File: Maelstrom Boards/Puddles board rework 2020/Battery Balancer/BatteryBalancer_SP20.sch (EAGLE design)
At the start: 84 parts, among them IC3 REG1117, P2 39-30-16, Q1 SPB80P06P, Q10 MOSFET-NCH-AO3404A, Q11 MOSFET-NCH-AO3404A, Q19 FDD4141TO252, Q2 SPB80P06P, Q22 FDD4141TO252, Q3 NMOSFET-D2PAK-7, Q4 310mA/60V/1.6Ω, Q5 NMOSFET-D2PAK-7, Q6 FDD4141TO252, Q7 MOSFET-NCH-AO3404A, Q8 MOSFET-NCH-AO3404A, Q9 MOSFET-NCH-AO3404A

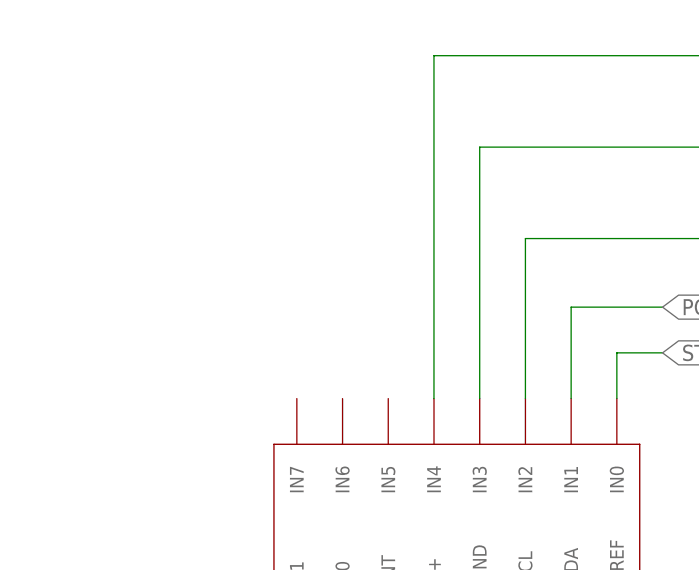
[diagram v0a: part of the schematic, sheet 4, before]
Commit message: final commit for ESC board, resistor values changed across boards for order ease
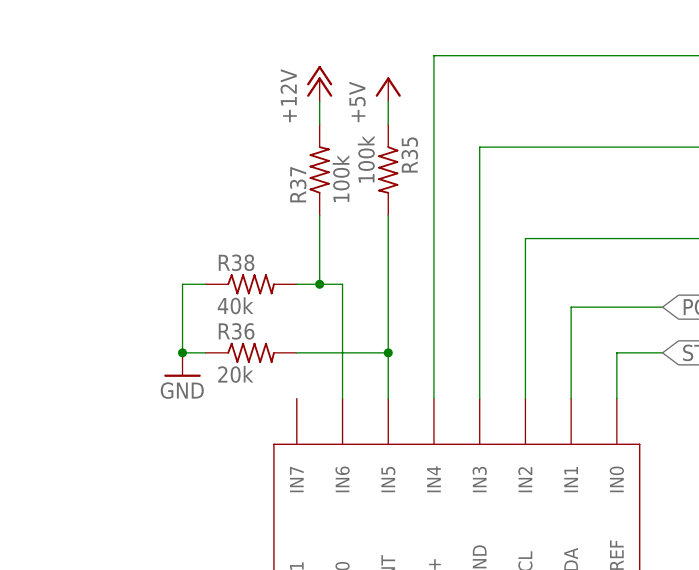
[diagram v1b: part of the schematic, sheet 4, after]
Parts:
- added R35, R37: 100k, rcl:R-US_R0603
- added R36: 20k, rcl:R-US_R0603
- added R38: 40k, rcl:R-US_R0603
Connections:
- new net N$31: R37.1, R38.2, U$12.IN6
- new net N$32: R35.2, R36.2, U$12.IN5
- net +12V: now also R37.2
- net +5V: now also R35.1
- net GND: now also R36.1, R38.1
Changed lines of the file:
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@@
 <part name="U$13" library="Vertical_Connectors" deviceset="6PIN-VERT" device=""/>
 <part name="GND26" library="supply1" library_urn="urn:adsk.eagle:library:371" deviceset="GND" device=""/>
+<part name="R35" library="rcl" library_urn="urn:adsk.eagle:library:334" deviceset="R-US_" device="R0603" package3d_urn="urn:adsk.eagle:package:23555/2" value="100k"/>
+<part name="R36" library="rcl" library_urn="urn:adsk.eagle:library:334" deviceset="R-US_" device="R0603" package3d_urn="urn:adsk.eagle:package:23555/2" value="20k"/>
+<part name="R37" library="rcl" library_urn="urn:adsk.eagle:library:334" deviceset="R-US_" device="R0603" package3d_urn="urn:adsk.eagle:package:23555/2" value="100k"/>
+<part name="R38" library="rcl" library_urn="urn:adsk.eagle:library:334" deviceset="R-US_" device="R0603" package3d_urn="urn:adsk.eagle:package:23555/2" value="40k"/>
+<part name="P+3" library="supply1" library_urn="urn:adsk.eagle:library:371" deviceset="+12V" device=""/>
+<part name="P+13" library="supply1" library_urn="urn:adsk.eagle:library:371" deviceset="+5V" device=""/>
+<part name="GND27" library="supply1" library_urn="urn:adsk.eagle:library:371" deviceset="GND" device=""/>
 </parts>
 <sheets>
@@
 <attribute name="VALUE" x="287.02" y="154.94" size="1.778" layer="96"/>
 </instance>
+<instance part="R35" gate="G$1" x="190.5" y="160.02" smashed="yes" rot="R270">
+<attribute name="NAME" x="191.9986" y="163.83" size="1.778" layer="95" rot="R270"/>
+<attribute name="VALUE" x="187.198" y="163.83" size="1.778" layer="96" rot="R270"/>
+</instance>
+<instance part="R36" gate="G$1" x="175.26" y="139.7" smashed="yes">
+<attribute name="NAME" x="171.45" y="141.1986" size="1.778" layer="95"/>
+<attribute name="VALUE" x="171.45" y="136.398" size="1.778" layer="96"/>
+</instance>
+<instance part="R37" gate="G$1" x="182.88" y="160.02" smashed="yes" rot="R90">
+<attribute name="NAME" x="181.3814" y="156.21" size="1.778" layer="95" rot="R90"/>
+<attribute name="VALUE" x="186.182" y="156.21" size="1.778" layer="96" rot="R90"/>
+</instance>
+<instance part="R38" gate="G$1" x="175.26" y="147.32" smashed="yes">
+<attribute name="NAME" x="171.45" y="148.8186" size="1.778" layer="95"/>
+<attribute name="VALUE" x="171.45" y="144.018" size="1.778" layer="96"/>
+</instance>
+<instance part="P+3" gate="1" x="182.88" y="170.18" smashed="yes">
+<attribute name="VALUE" x="180.34" y="165.1" size="1.778" layer="96" rot="R90"/>
+</instance>
+<instance part="P+13" gate="1" x="190.5" y="170.18" smashed="yes">
+<attribute name="VALUE" x="187.96" y="165.1" size="1.778" layer="96" rot="R90"/>
+</instance>
+<instance part="GND27" gate="1" x="167.64" y="137.16" smashed="yes">
+<attribute name="VALUE" x="165.1" y="134.62" size="1.778" layer="96"/>
+</instance>
 </instances>
 <busses>
@@
 <pinref part="GND5" gate="1" pin="GND"/>
 </segment>
+<segment>
+<pinref part="R36" gate="G$1" pin="1"/>
+<wire x1="170.18" y1="139.7" x2="167.64" y2="139.7" width="0.1524" layer="91"/>
+<pinref part="R38" gate="G$1" pin="1"/>
+<wire x1="167.64" y1="139.7" x2="167.64" y2="147.32" width="0.1524" layer="91"/>
+<wire x1="167.64" y1="147.32" x2="170.18" y2="147.32" width="0.1524" layer="91"/>
+<pinref part="GND27" gate="1" pin="GND"/>
+<junction x="167.64" y="139.7"/>
+</segment>
 </net>
 <net name="PORT_BATTERY" class="0">
@@
 </segment>
 </net>
+<net name="N$31" class="0">
+<segment>
+<pinref part="R38" gate="G$1" pin="2"/>
+<wire x1="180.34" y1="147.32" x2="182.88" y2="147.32" width="0.1524" layer="91"/>
+<pinref part="R37" gate="G$1" pin="1"/>
+<wire x1="182.88" y1="147.32" x2="182.88" y2="154.94" width="0.1524" layer="91"/>
+<pinref part="U$12" gate="G$1" pin="IN6"/>
+<wire x1="185.42" y1="134.62" x2="185.42" y2="147.32" width="0.1524" layer="91"/>
+<wire x1="185.42" y1="147.32" x2="182.88" y2="147.32" width="0.1524" layer="91"/>
+<junction x="182.88" y="147.32"/>
+</segment>
+</net>
+<net name="N$32" class="0">
+<segment>
+<pinref part="R35" gate="G$1" pin="2"/>
+<wire x1="190.5" y1="154.94" x2="190.5" y2="139.7" width="0.1524" layer="91"/>
+<pinref part="R36" gate="G$1" pin="2"/>
+<wire x1="190.5" y1="139.7" x2="180.34" y2="139.7" width="0.1524" layer="91"/>
+<pinref part="U$12" gate="G$1" pin="IN5"/>
+<wire x1="190.5" y1="134.62" x2="190.5" y2="139.7" width="0.1524" layer="91"/>
+<junction x="190.5" y="139.7"/>
+</segment>
+</net>
+<net name="+12V" class="0">
+<segment>
+<pinref part="R37" gate="G$1" pin="2"/>
+<pinref part="P+3" gate="1" pin="+12V"/>
+<wire x1="182.88" y1="167.64" x2="182.88" y2="165.1" width="0.1524" layer="91"/>
+</segment>
+</net>
+<net name="+5V" class="0">
+<segment>
+<pinref part="R35" gate="G$1" pin="1"/>
+<pinref part="P+13" gate="1" pin="+5V"/>
+<wire x1="190.5" y1="167.64" x2="190.5" y2="165.1" width="0.1524" layer="91"/>
+</segment>
+</net>

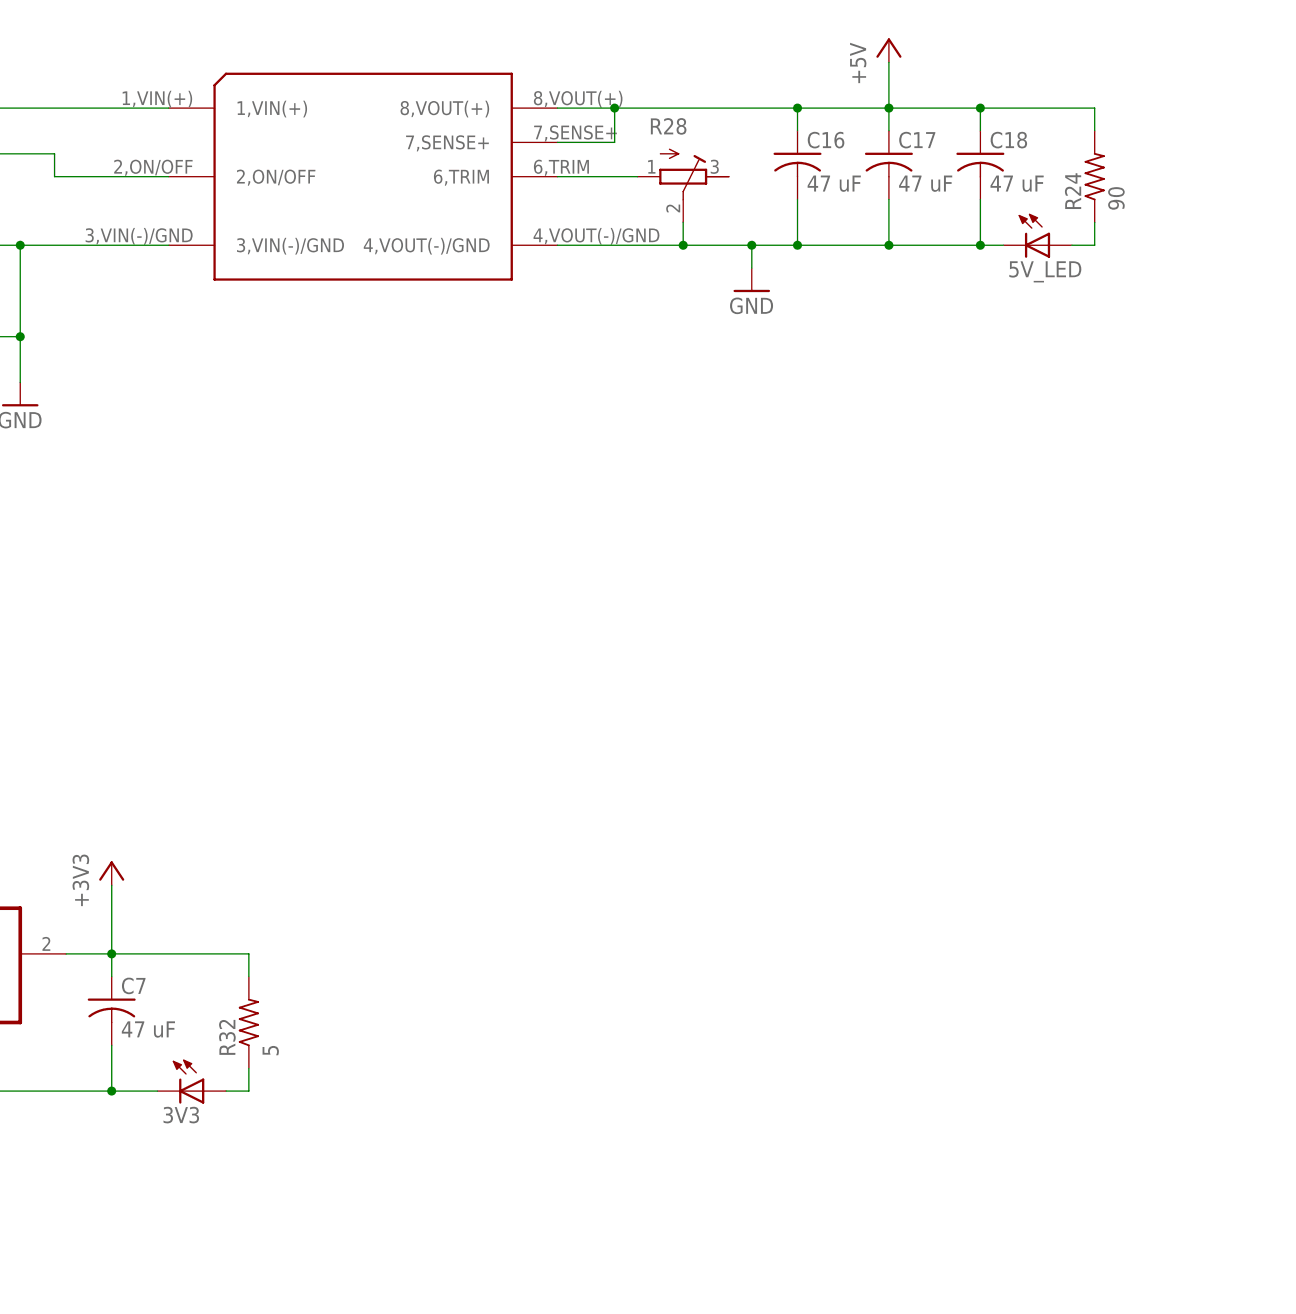
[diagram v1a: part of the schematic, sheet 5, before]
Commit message: Changing puddles values
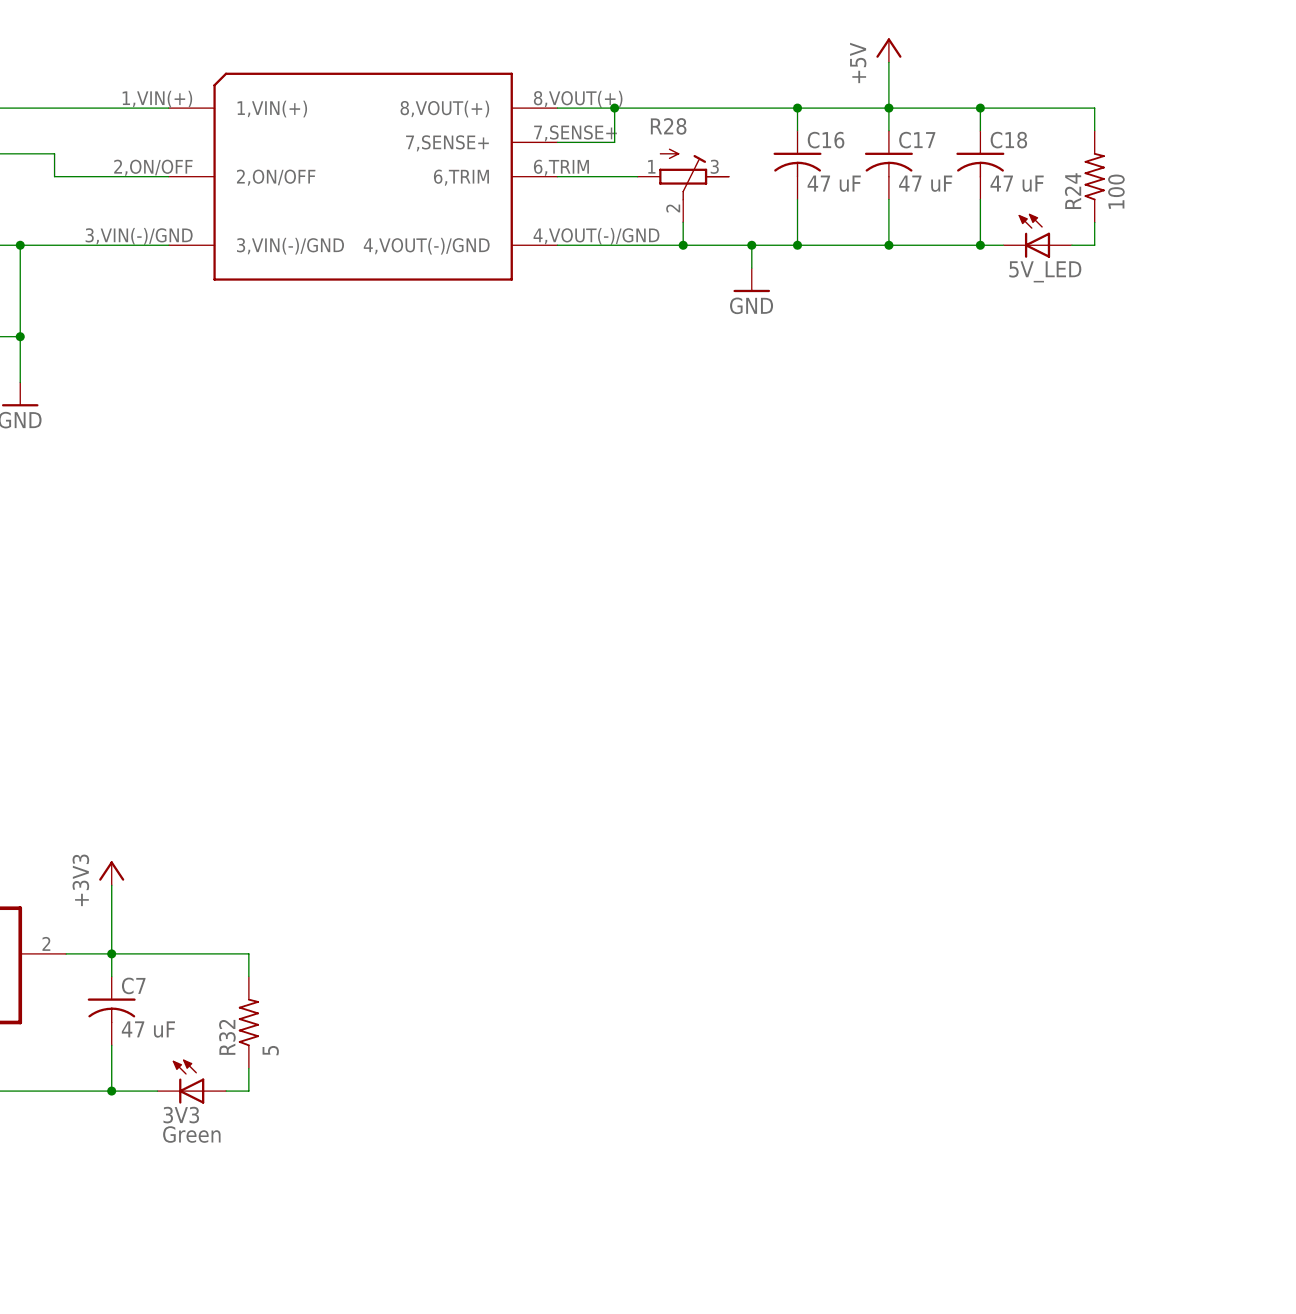
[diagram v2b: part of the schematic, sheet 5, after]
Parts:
- 3V3: value (none) -> Green
- R24: value 90 -> 100
- R38: value 40k -> 39k
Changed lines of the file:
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@@
 <?xml version="1.0" encoding="utf-8"?>
 <!DOCTYPE eagle SYSTEM "eagle.dtd">
-<eagle version="9.5.2">
+<eagle version="9.6.2">
 <drawing>
 <settings>
@@
 <part name="C12" library="rcl" library_urn="urn:adsk.eagle:library:334" deviceset="CPOL-US" device="E5-10.5" package3d_urn="urn:adsk.eagle:package:23372/1" value="330 uF"/>
 <part name="P+12" library="supply1" library_urn="urn:adsk.eagle:library:371" deviceset="V+" device=""/>
-<part name="R24" library="rcl" library_urn="urn:adsk.eagle:library:334" deviceset="R-US_" device="R0603" package3d_urn="urn:adsk.eagle:package:23555/2" value="90"/>
+<part name="R24" library="rcl" library_urn="urn:adsk.eagle:library:334" deviceset="R-US_" device="R0603" package3d_urn="urn:adsk.eagle:package:23555/2" value="100"/>
 <part name="5V_LED" library="led" library_urn="urn:adsk.eagle:library:259" deviceset="LED" device="CHIPLED_0603" package3d_urn="urn:adsk.eagle:package:15822/2"/>
 <part name="P+15" library="supply1" library_urn="urn:adsk.eagle:library:371" deviceset="+12V" device=""/>
@@
 <part name="C21" library="resistor" library_urn="urn:adsk.eagle:library:348" deviceset="C-US" device="C1206K" package3d_urn="urn:adsk.eagle:package:26202/1" value="47 uF"/>
 <part name="R32" library="rcl" library_urn="urn:adsk.eagle:library:334" deviceset="R-US_" device="R0603" package3d_urn="urn:adsk.eagle:package:23555/2" value="5"/>
-<part name="3V3" library="led" library_urn="urn:adsk.eagle:library:259" deviceset="LED" device="CHIPLED_0603" package3d_urn="urn:adsk.eagle:package:15822/2"/>
+<part name="3V3" library="led" library_urn="urn:adsk.eagle:library:259" deviceset="LED" device="CHIPLED_0603" package3d_urn="urn:adsk.eagle:package:15822/2" value="Green"/>
 <part name="Q9" library="SparkFun-DiscreteSemi" deviceset="MOSFET-NCH" device="-AO3404A" value=""/>
 <part name="Q10" library="SparkFun-DiscreteSemi" deviceset="MOSFET-NCH" device="-AO3404A" value=""/>
@@
 <part name="R36" library="rcl" library_urn="urn:adsk.eagle:library:334" deviceset="R-US_" device="R0603" package3d_urn="urn:adsk.eagle:package:23555/2" value="20k"/>
 <part name="R37" library="rcl" library_urn="urn:adsk.eagle:library:334" deviceset="R-US_" device="R0603" package3d_urn="urn:adsk.eagle:package:23555/2" value="100k"/>
-<part name="R38" library="rcl" library_urn="urn:adsk.eagle:library:334" deviceset="R-US_" device="R0603" package3d_urn="urn:adsk.eagle:package:23555/2" value="40k"/>
+<part name="R38" library="rcl" library_urn="urn:adsk.eagle:library:334" deviceset="R-US_" device="R0603" package3d_urn="urn:adsk.eagle:package:23555/2" value="39k"/>
 <part name="P+3" library="supply1" library_urn="urn:adsk.eagle:library:371" deviceset="+12V" device=""/>
 <part name="P+13" library="supply1" library_urn="urn:adsk.eagle:library:371" deviceset="+5V" device=""/>

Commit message: updates to puddles board rework actuator and BB.
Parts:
- added C14: 1000 uF, rcl:CPOL-USE5-13
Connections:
- net +12V: now also U$13.1+
- net BALANCED_OUT: now also C14.+; no longer U$13.1+
- net GND: now also C14.-
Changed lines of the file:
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@@
 <?xml version="1.0" encoding="utf-8"?>
 <!DOCTYPE eagle SYSTEM "eagle.dtd">
-<eagle version="9.6.2">
+<eagle version="9.5.2">
 <drawing>
 <settings>
@@
 <part name="P+13" library="supply1" library_urn="urn:adsk.eagle:library:371" deviceset="+5V" device=""/>
 <part name="GND27" library="supply1" library_urn="urn:adsk.eagle:library:371" deviceset="GND" device=""/>
+<part name="P+16" library="supply1" library_urn="urn:adsk.eagle:library:371" deviceset="+12V" device=""/>
+<part name="C14" library="rcl" library_urn="urn:adsk.eagle:library:334" deviceset="CPOL-US" device="E5-13" package3d_urn="urn:adsk.eagle:package:23375/1" value="1000 uF"/>
 </parts>
 <sheets>
@@
 <attribute name="VALUE" x="337.82" y="187.96" size="1.778" layer="96"/>
 </instance>
+<instance part="P+16" gate="1" x="289.56" y="190.5" smashed="yes" rot="R90">
+<attribute name="VALUE" x="294.64" y="187.96" size="1.778" layer="96" rot="R180"/>
+</instance>
+<instance part="C14" gate="G$1" x="309.88" y="210.82" smashed="yes" rot="R90">
+<attribute name="NAME" x="309.245" y="211.836" size="1.778" layer="95" rot="R90"/>
+<attribute name="VALUE" x="314.071" y="211.836" size="1.778" layer="96" rot="R90"/>
+</instance>
 </instances>
 <busses>
@@
 <wire x1="322.58" y1="195.58" x2="332.74" y2="195.58" width="0.1524" layer="91"/>
 <junction x="332.74" y="195.58"/>
+<pinref part="C14" gate="G$1" pin="-"/>
+<wire x1="332.74" y1="200.66" x2="332.74" y2="210.82" width="0.1524" layer="91"/>
+<wire x1="332.74" y1="210.82" x2="314.96" y2="210.82" width="0.1524" layer="91"/>
+<junction x="332.74" y="200.66"/>
 </segment>
 <segment>
@@
 <pinref part="P+11" gate="1" pin="+12V"/>
 </segment>
+<segment>
+<pinref part="U$13" gate="G$1" pin="1+"/>
+<wire x1="302.26" y1="190.5" x2="292.1" y2="190.5" width="0.1524" layer="91"/>
+<pinref part="P+16" gate="1" pin="+12V"/>
+</segment>
 </net>
 <net name="MOBO_SWITCHED" class="0">
@@
 <net name="BALANCED_OUT" class="0">
 <segment>
-<pinref part="U$13" gate="G$1" pin="1+"/>
-<wire x1="302.26" y1="190.5" x2="292.1" y2="190.5" width="0.1524" layer="91"/>
-<wire x1="292.1" y1="190.5" x2="292.1" y2="195.58" width="0.1524" layer="91"/>
 <pinref part="U$13" gate="G$1" pin="3+"/>
 <wire x1="292.1" y1="195.58" x2="292.1" y2="200.66" width="0.1524" layer="91"/>
@@
 <wire x1="292.1" y1="195.58" x2="284.48" y2="195.58" width="0.1524" layer="91"/>
 <label x="284.48" y="195.58" size="1.778" layer="95" rot="R180" xref="yes"/>
+<pinref part="C14" gate="G$1" pin="+"/>
+<wire x1="292.1" y1="200.66" x2="292.1" y2="210.82" width="0.1524" layer="91"/>
+<wire x1="292.1" y1="210.82" x2="307.34" y2="210.82" width="0.1524" layer="91"/>
+<junction x="292.1" y="200.66"/>
 </segment>
 </net>
